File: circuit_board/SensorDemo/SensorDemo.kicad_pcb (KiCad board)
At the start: 4 copper layers, 65 x 57.5 mm, 58 parts, among them K1 PB, P1 CONN3X2, P2 CONN3X2, U1 TLV1117-33CDCYR, U2 dsPIC33EP32GP502, U3 LTC1658, U4 INA126, U5 REF1925, U6 REF1925, X1 8MHz

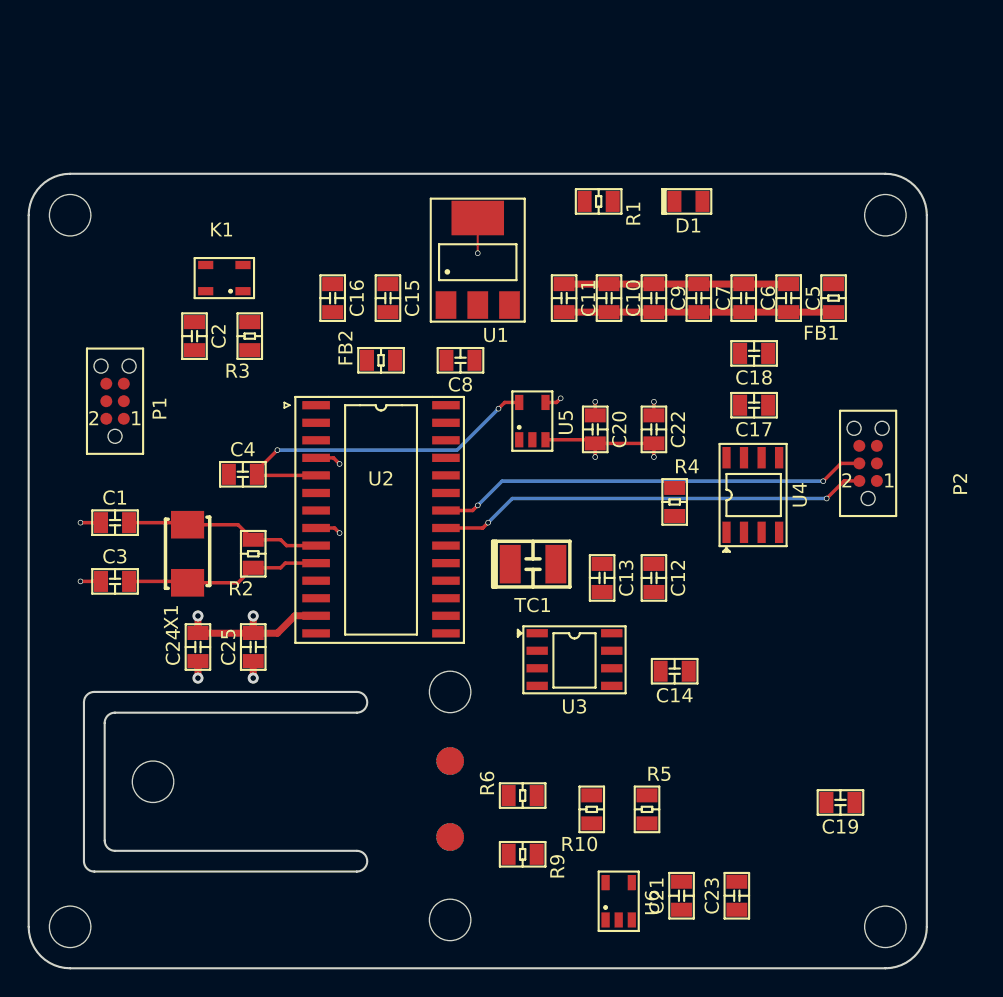
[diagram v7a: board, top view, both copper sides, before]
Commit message: SensorDemo board updated
re-positioned all components and routed pcb.
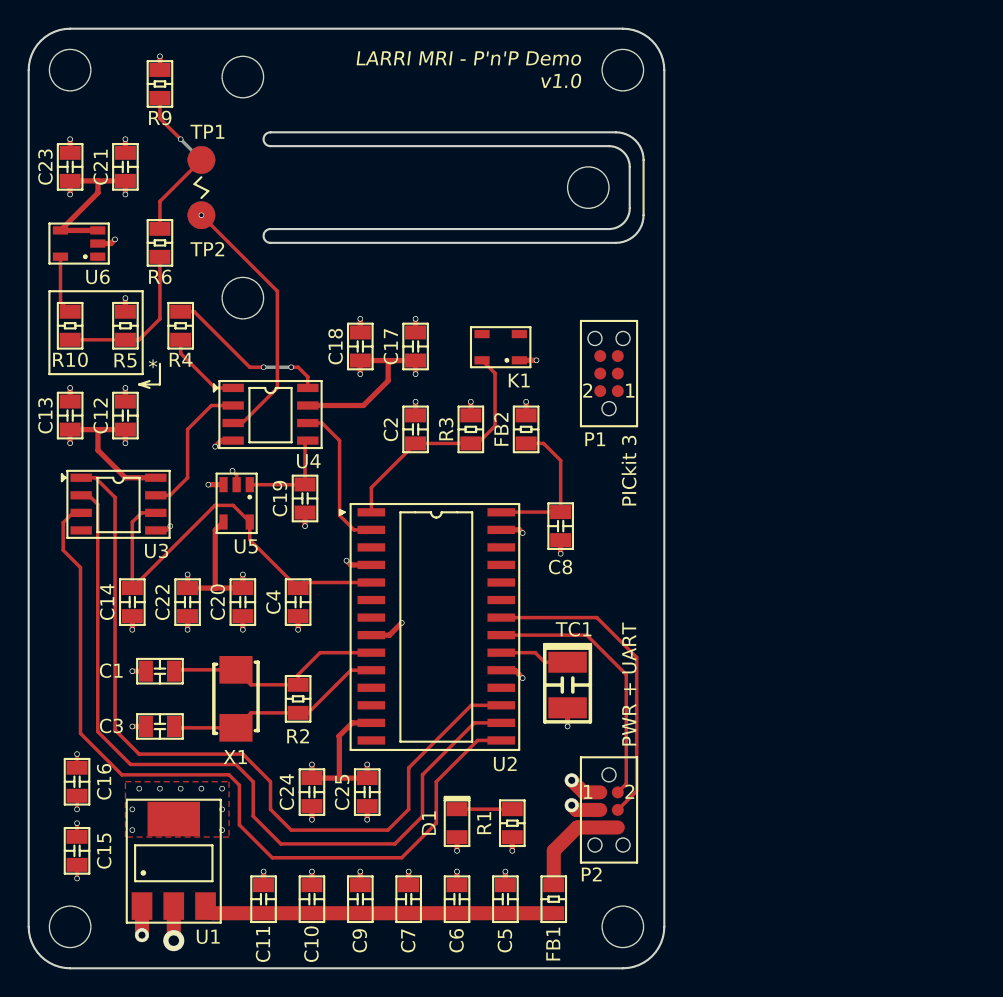
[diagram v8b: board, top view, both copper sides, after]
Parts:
- added G***: LOGO, SensorDemo_pcb:logo_RZ_short, B.Cu at (133.0, 122.0)
- moved C23 71.5 mm to (120.5, 67.0), turned to 90 degrees
- moved C21 66.4 mm to (124.5, 67.0), turned to 90 degrees
- moved R9 61.6 mm to (127.0, 61.0), turned to 90 degrees
- moved U6 60.5 mm to (122.5, 73.5), turned to 180 degrees
- moved MH6 53.3 mm to (158.0, 68.5), turned to 0 degrees
- moved TP1 52.2 mm to (130.0, 66.5)
- moved TP4 52.2 mm to (130.0, 66.5)
- moved R10 51.5 mm to (120.5, 78.5), turned to 90 degrees
- moved R5 51.5 mm to (124.5, 78.5), turned to 270 degrees
- moved U1 48.7 mm to (128.0, 120.5)
- moved C11 48.6 mm to (134.5, 120.0)
- moved C10 48.5 mm to (138.0, 120.0)
- moved C9 48.4 mm to (141.5, 120.0)
- moved C7 48.3 mm to (145.0, 120.0)
- moved C6 48.2 mm to (148.5, 120.0)
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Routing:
- net Net-(U2-Pad15): track 0.00 -> 58.5 mm
- net Net-(U2-Pad17): track 0.00 -> 57.5 mm
- net Net-(U2-Pad16): track 0.00 -> 57.3 mm
- net +3V3: track 24.1 -> 73.0 mm, vias 6 -> 27
- net GND: track 27.4 -> 49.0 mm, vias 8 -> 40
- net /Vsen: track 0.00 -> 19.0 mm, vias 0 -> 1
- net Net-(C2-Pad1): track 0.00 -> 17.7 mm
- net /ucTX: track 31.3 -> 19.0 mm, vias 2 -> 0
- net Net-(R4-Pad2): track 0.00 -> 12.0 mm, vias 0 -> 2
- net Net-(R10-Pad1): track 0.00 -> 11.6 mm
- net Net-(C8-Pad1): track 0.00 -> 11.1 mm
- net /sensVal: track 0.00 -> 11.0 mm
- net Net-(U3-Pad7): track 0.00 -> 10.3 mm
- net /ucRX: track 31.3 -> 22.6 mm, vias 2 -> 0
- net Net-(FB1-Pad1): track 0.00 -> 7.82 mm
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- added copper zone on F.Cu, net +3V3
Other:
- board size 65 x 57.5 mm -> 46 x 68 mm
- net class 3V3 added: clearance 0.254, trace_width 0.381, via_dia 0.4, via_drill 0.3
- net class Default: clearance 0.1524 -> 0.254; trace_width 0.1524 -> 0.254
- net class GND added: clearance 0.254, trace_width 0.381, via_dia 0.4, via_drill 0.3
- rule trace_clearance: 0.1524 -> 0.254
- board text added: "*"
- board text added: "* R5: LDO 3.3V R10: REF19xx"
- board text added: "1 GND 2 TX 3 GND 4 RX 5 VCC 6 VCC"
- board text added: "1 ~MCLR 2 VDD 3 GND 4 PGD 5 PGC 6 N.C."
- board text added: "Daniel & Ruoshi"
- board text added: "LARRI MRI - P'n'P Demo v1.0"
- board text added: "PICkit 3"
- board text added: "PWR + UART"
